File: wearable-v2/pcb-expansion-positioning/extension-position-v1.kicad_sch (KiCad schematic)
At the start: 17 parts, among them IC1 TESEO-LIV3F, J8 HERALD_V2_CONN_PLUG, U14 LIS2DE12

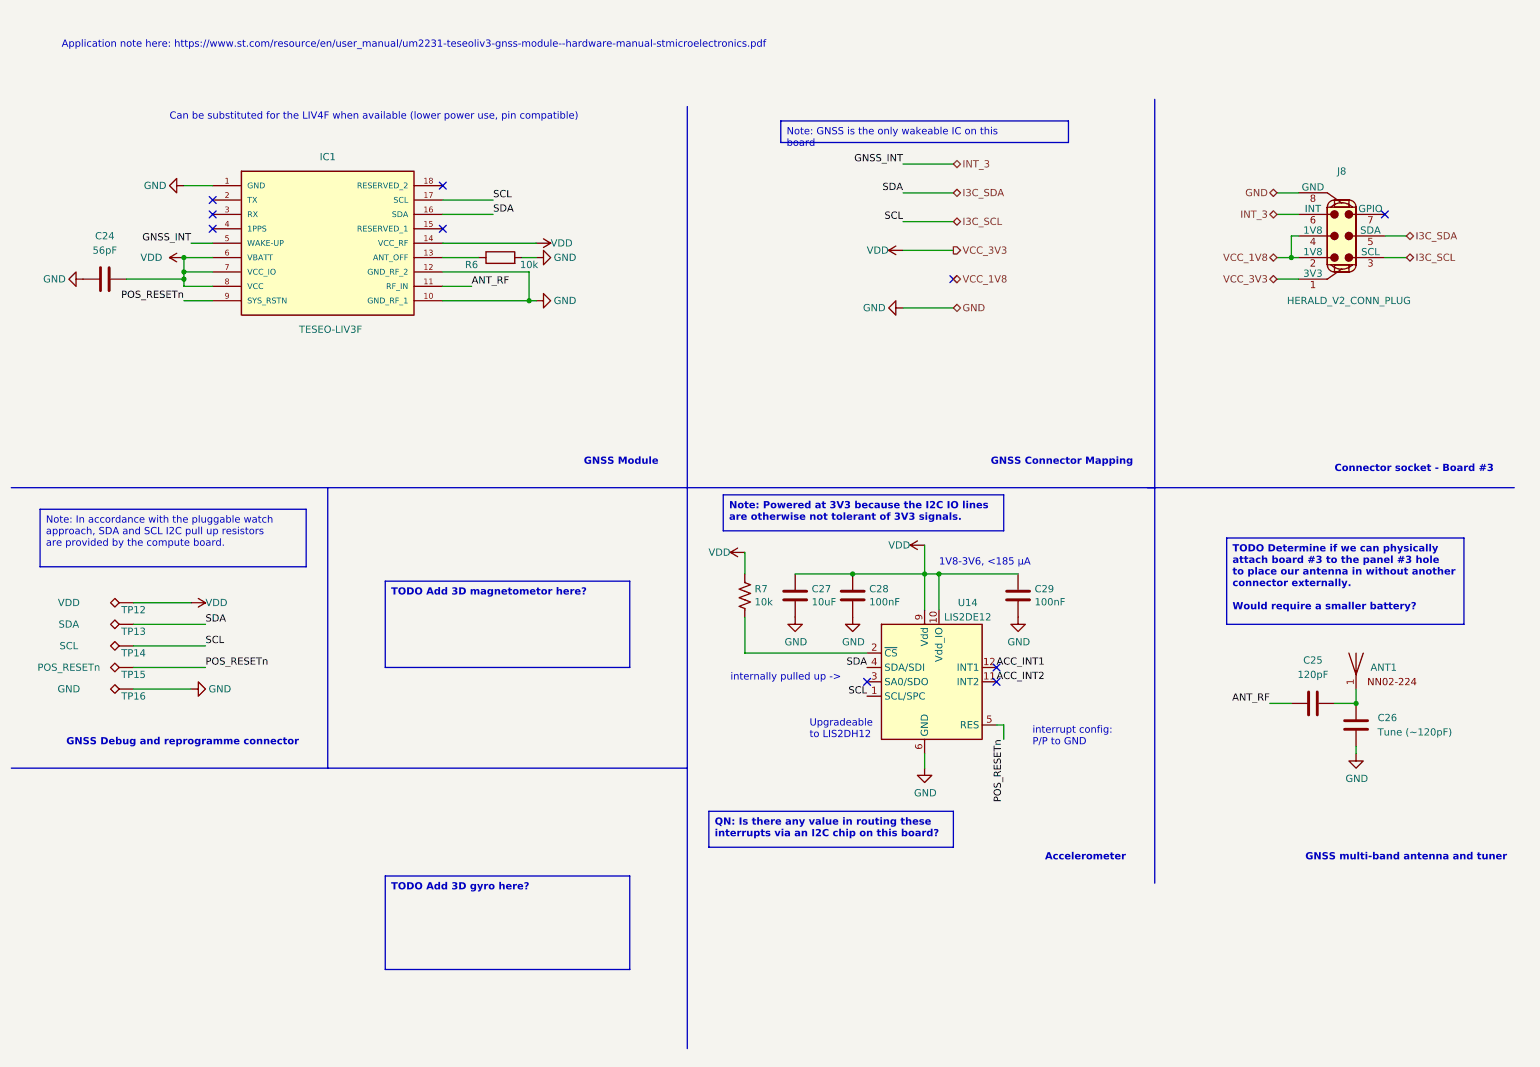
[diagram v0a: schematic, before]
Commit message: Reworked boards for JLCPCB manufacture
Slightly larger Vias.
Added debug pin holes for Beta testing.
Signed-off-by: Adam Fowler <adam@adamfowler.org>
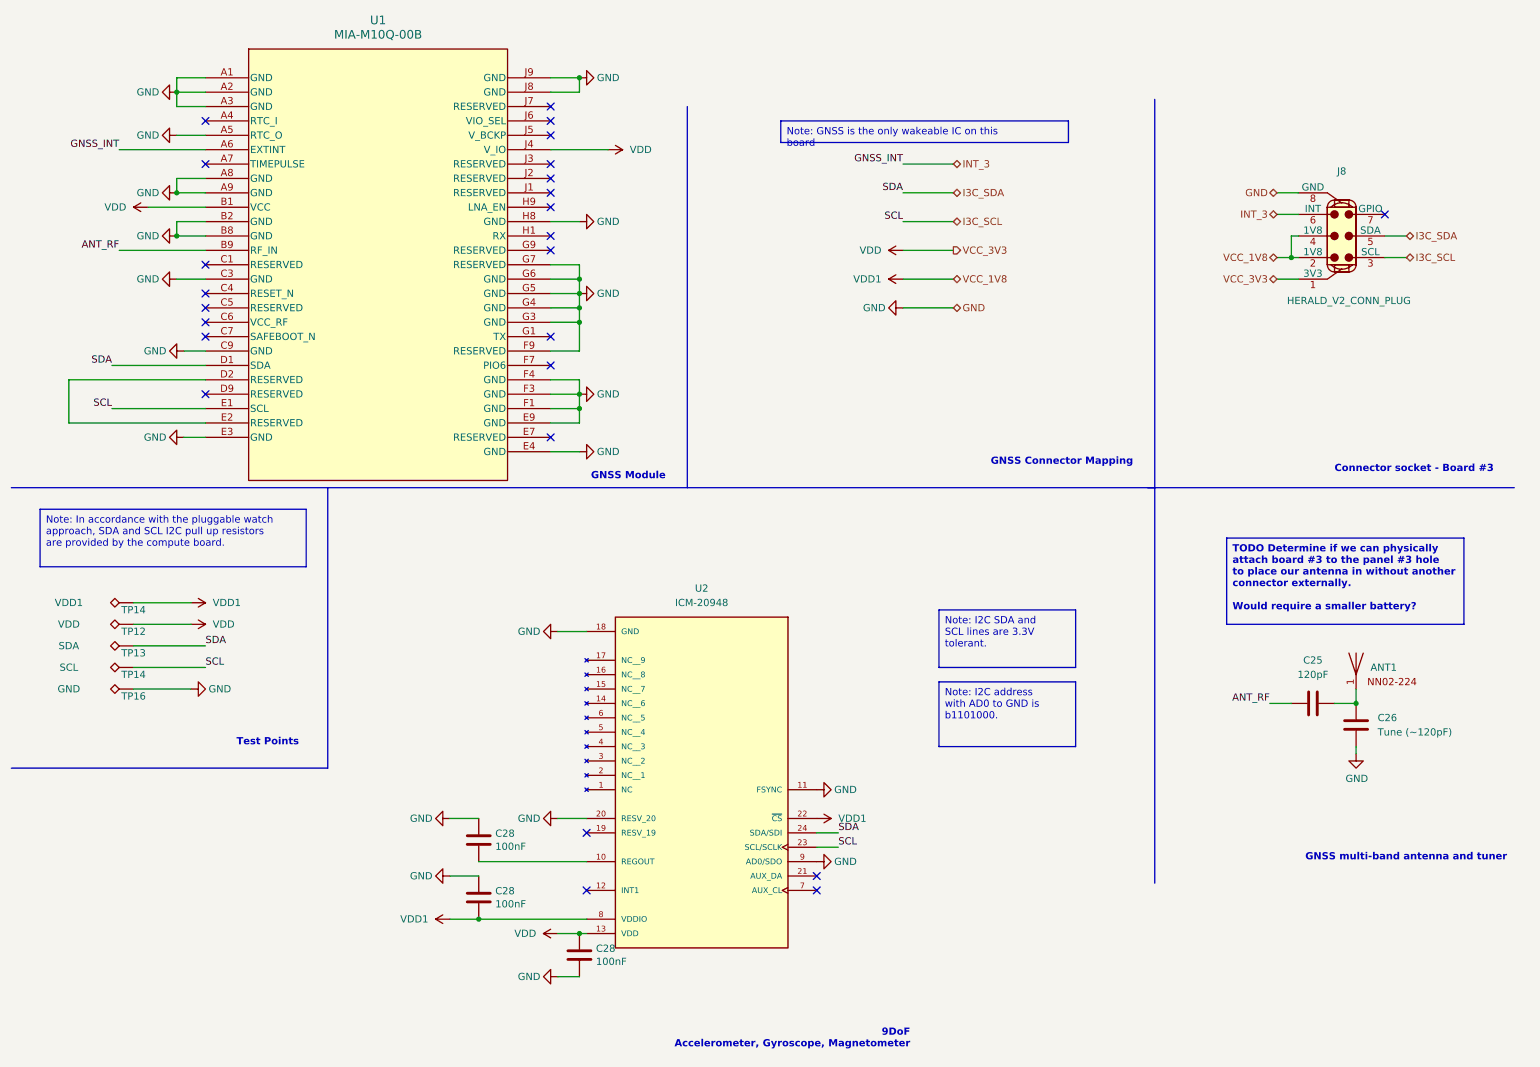
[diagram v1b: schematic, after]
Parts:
- removed C24: 56pF, Capacitor_SMD:C_0402_1005Metric, symbol Device:C
- removed C27: 10uF, Capacitor_SMD:C_0402_1005Metric, symbol Device:C
- removed C28, C29: 100nF, Capacitor_SMD:C_0402_1005Metric, symbol Device:C
- removed IC1: TESEO-LIV3F, SON110P970X1010X230-18N, symbol Herald_Extras:TESEO-LIV3F
- removed R6: 10k, Resistor_SMD:R_0402_1005Metric, symbol Device:R
- removed R7: 10k, Resistor_SMD:R_0402_1005Metric, symbol Device:R_US
- removed TP15: POS_RESETn, TestPoint:TestPoint_Pad_D1.0mm, symbol Connector:TestPoint_Alt
- removed U14: LIS2DE12, Package_LGA:LGA-12_2x2mm_P0.5mm, symbol Sensor_Motion:LIS2DE12
- added C28 (x3): 100nF, Capacitor_SMD:C_0402_1005Metric, symbol Device:C
- added TP14: VDD1, TestPoint:TestPoint_Pad_D1.0mm, symbol Connector:TestPoint_Alt
- added U1: MIA-M10Q-00B, Herald:LGA_M10Q-00B_UBL, symbol Herald_Extras:MIA-M10Q-00B
- added U2: ICM-20948, Herald:ICM-20948-QFN40P300X300X105-24N, symbol Herald_Extras:ICM-20948
- ANT1: MPN (none) -> NN02-224; Manufacturer (none) -> Ignion
- C25, C26: MPN (none) -> GRM1555C2A121GE01D
- J8: footprint (none) -> Herald:HERALD_V2_CONN_PORT; MPN (none) -> 145861006024829+; Manufacturer (none) -> Kyocera
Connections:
- net VCC_1V8 is gone; now on net VDD1: J8.2 (1V8), J8.4 (1V8)
- net ANT_RF: now also U1.B9 (RF_IN)
- net GND: now also C28.1, C28.1, C28.2, U1.A1 (GND), U1.A2 (GND), U1.A3 (GND), U1.A5 (RTC_O), U1.A8 (GND), U1.A9 (GND), U1.B2 (GND), U1.B8 (GND), U1.C3 (GND), U1.C9 (GND), U1.E3 (GND), U1.E4 (GND), U1.E9 (GND), U1.F1 (GND), U1.F3 (GND), U1.F4 (GND), U1.F9 (RESERVED), U1.G3 (GND), U1.G4 (GND), U1.G5 (GND), U1.G6 (GND), U1.G7 (RESERVED), U1.H8 (GND), U1.J8 (GND), U1.J9 (GND), U2.11 (FSYNC), U2.18 (GND), U2.20 (RESV_20), U2.9 (AD0/SDO)
- net I3C_SCL: now also U1.E1 (SCL), U2.23 (SCL/SCLK)
- net I3C_SDA: now also U1.D1 (SDA), U2.24 (SDA/SDI)
- net INT_3: now also U1.A6 (EXTINT)
- net VDD1: now also C28.2, TP14.1, U2.22 (~{CS}), U2.8 (VDDIO); no longer J8.1 (3V3), TP12.1
- new net: C28.2, U2.10 (REGOUT)
- new net: U1.D2 (RESERVED), U1.E2 (RESERVED)
- new net VDD: C28.1, J8.1 (3V3), TP12.1, U1.B1 (VCC), U1.J4 (V_IO), U2.13 (VDD)
- no-connect marks 10 -> 25
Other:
- note added: "9DoF Accelerometer, Gyroscope, Magnetometer"
- note added: "Test Points"
- note removed: "1V8-3V6, <185 µA"
- note removed: "Accelerometer"
- note removed: "Application note here: https://www.st.com/resource/en/user_manual/um2231-teseoliv3-gnss-module--hardware-manual-stmicroelectronics.pdf"
- note removed: "Can be substituted for the LIV4F when available (lower power use, pin compatible)"
- note removed: "GNSS Debug and reprogramme connector"
- note removed: "Upgradeable to LIS2DH12"
- note removed: "internally pulled up ->"
- note removed: "interrupt config: P/P to GND"
- moved on the sheet: TP12, TP13, TP14

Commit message: Added Antenna panel and Micro connector boards
Micro connector uses the nPM1300 PMIC from Nordic Semi.
Signed-off-by: Adam Fowler <adam@adamfowler.org>
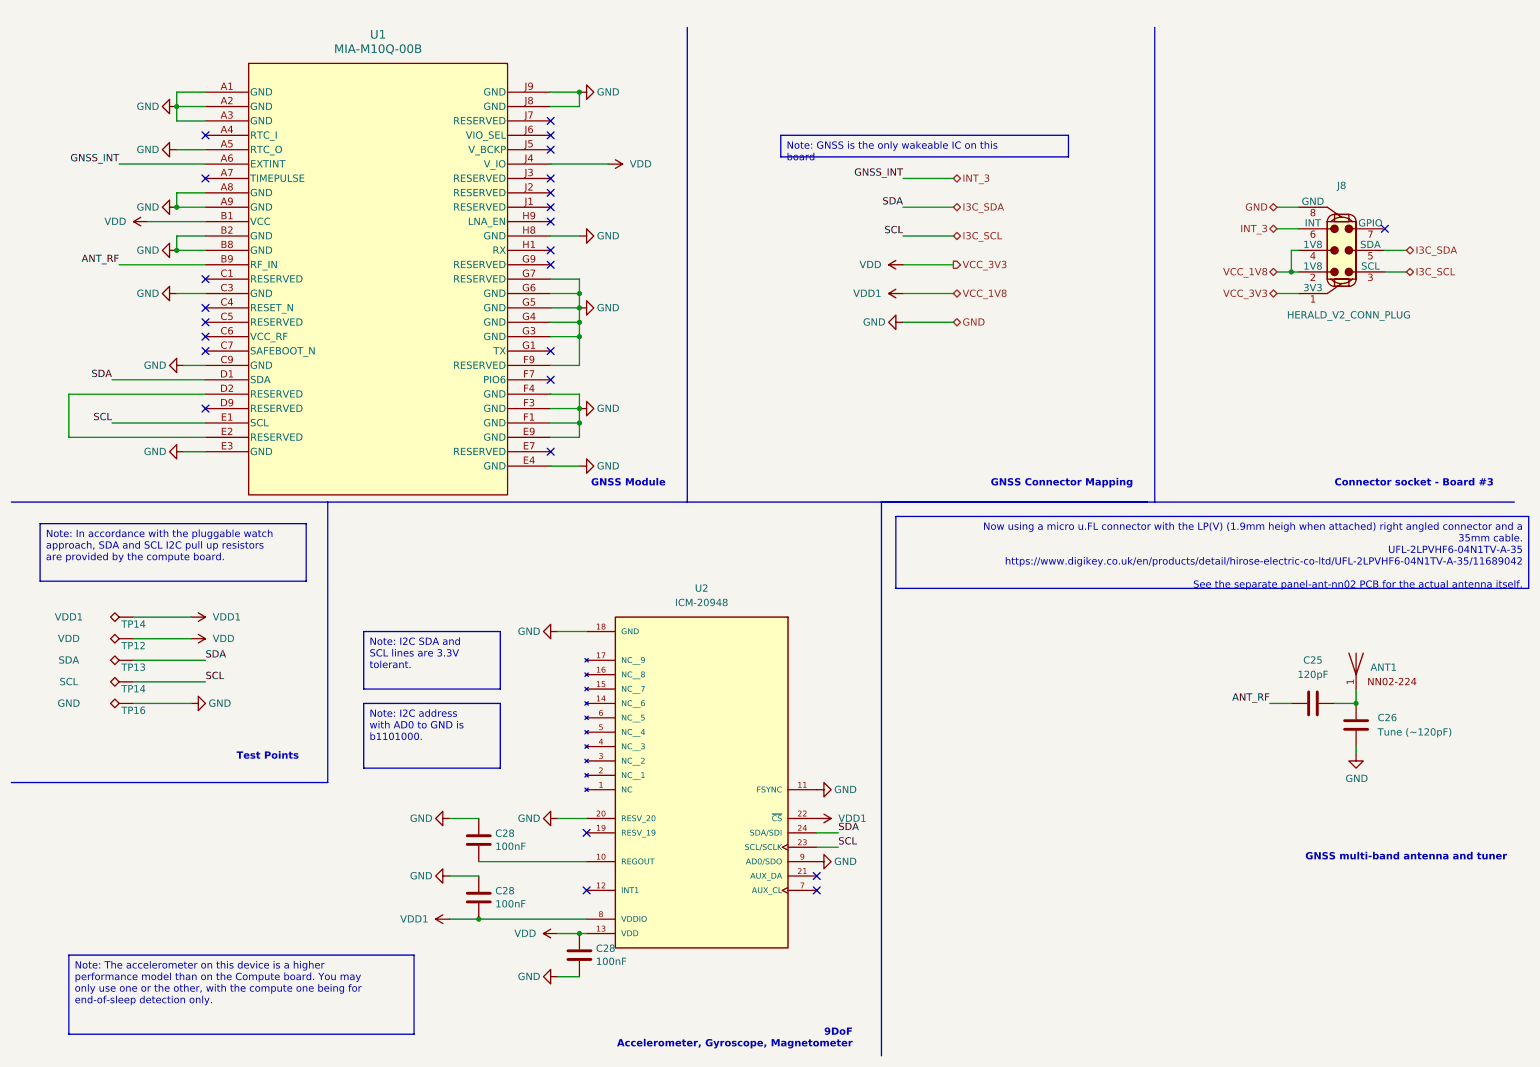
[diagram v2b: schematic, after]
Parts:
- ANT1: footprint Herald:NN02-224 -> Connector_Coaxial:U.FL_Hirose_U.FL-R-SMT-1_Vertical; MPN NN02-224 -> U.FL-R-SMT-1(60); Manufacturer Ignion -> Hirose Electric Co Ltd
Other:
- moved on the sheet: J8, TP12, TP13, TP14, TP16, U1
